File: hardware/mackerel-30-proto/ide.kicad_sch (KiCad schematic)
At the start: 11 parts, among them J12 Screw_Terminal_01x04, J13 Conn_02x20_Odd_Even, U12 74HC245, U13 74HC245

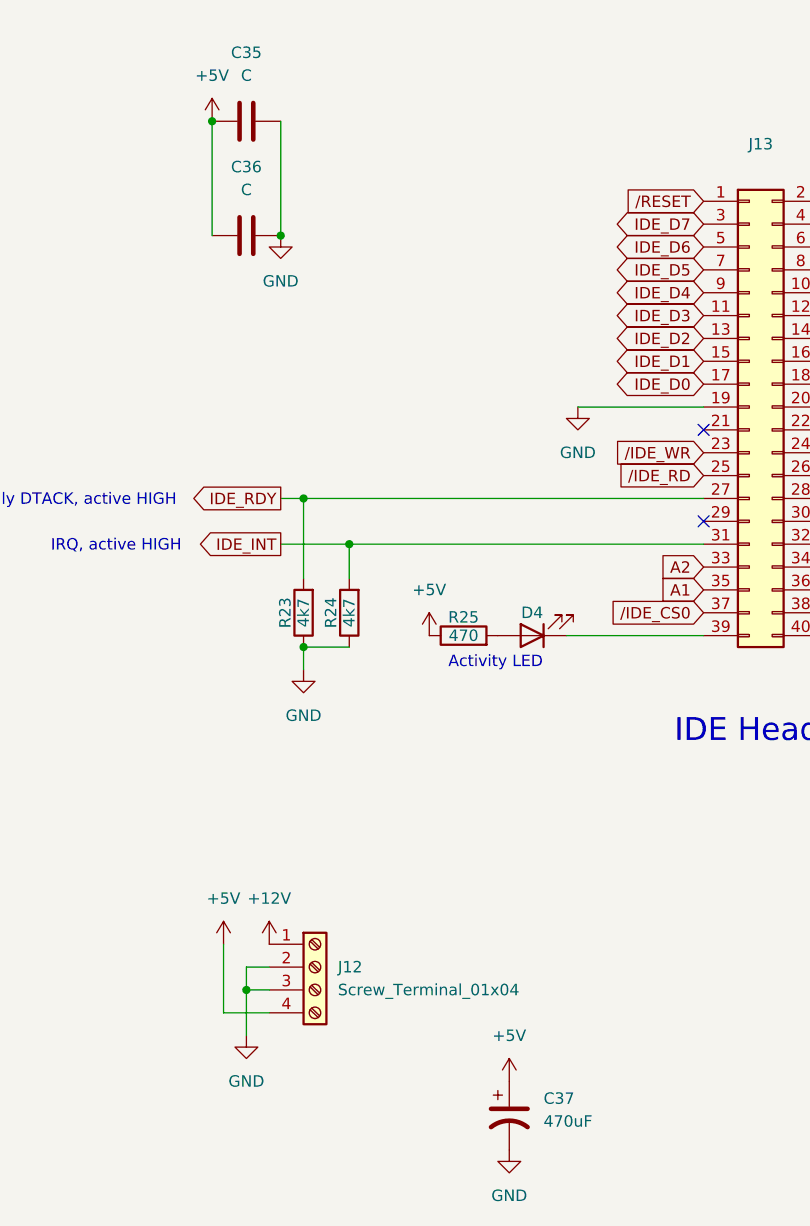
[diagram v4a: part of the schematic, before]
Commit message: Rough routing of data bus to FPU and RAM
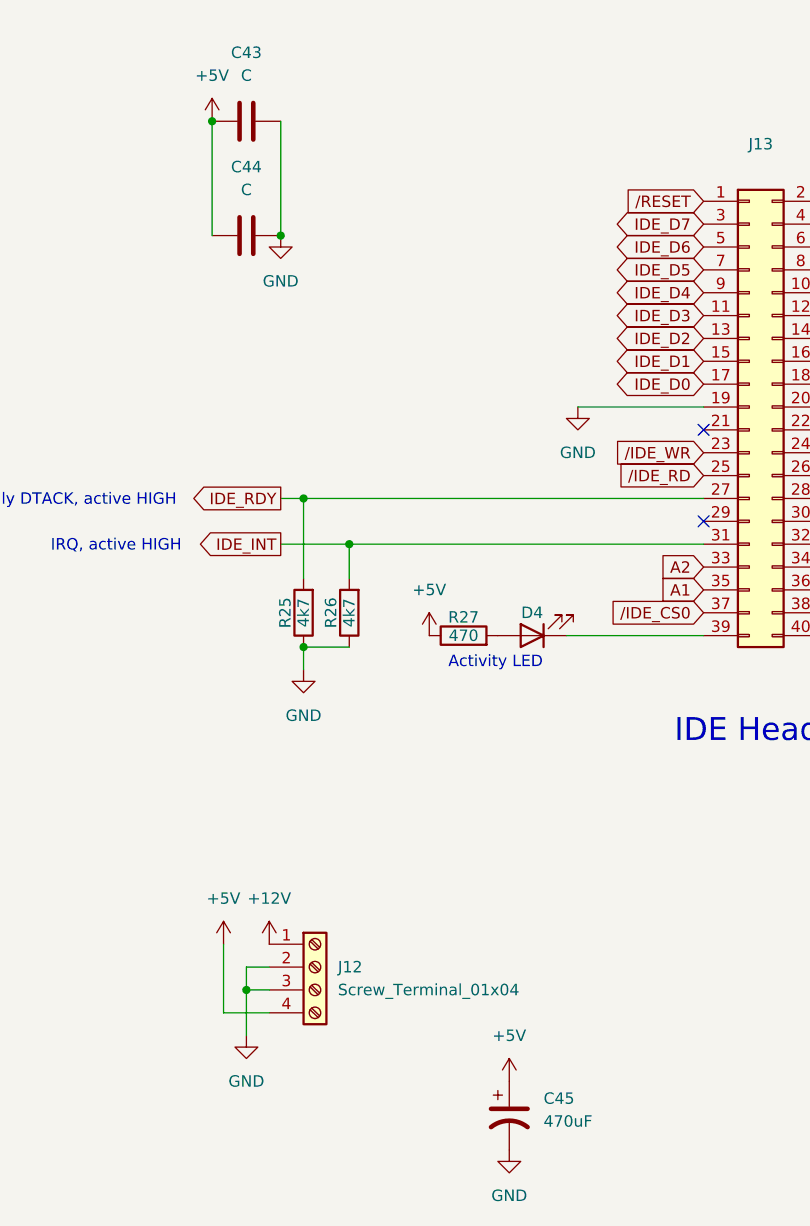
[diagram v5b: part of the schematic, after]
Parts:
- renumbered C35 to C43, C36 to C44, C37 to C45, R23 to R25, R24 to R26, R25 to R27
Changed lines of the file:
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@@
 		(dnp no)
 		(fields_autoplaced yes)
-		(property "Reference" "#PWR084"
+		(property "Reference" "#PWR086"
 			(at 175.26 151.13 0)
 			(effects
@@
 			(project "mackerel-30-proto"
 				(path "/9307474f-ec99-494d-b4c9-fbd0b10ce86a/b80ba0ac-a3c1-4262-b297-c092dfcb6fec"
-					(reference "#PWR084")
+					(reference "#PWR086")
 					(unit 1)
 				)
@@
 		(dnp no)
 		(fields_autoplaced yes)
-		(property "Reference" "#PWR073"
+		(property "Reference" "#PWR075"
 			(at 81.28 39.37 0)
 			(effects
@@
 			(project "mackerel-30-proto"
 				(path "/9307474f-ec99-494d-b4c9-fbd0b10ce86a/b80ba0ac-a3c1-4262-b297-c092dfcb6fec"
-					(reference "#PWR073")
+					(reference "#PWR075")
 					(unit 1)
 				)
@@
 		(dnp no)
 		(fields_autoplaced yes)
-		(property "Reference" "#PWR076"
+		(property "Reference" "#PWR078"
 			(at 81.28 156.21 0)
 			(effects
@@
 			(project "mackerel-30-proto"
 				(path "/9307474f-ec99-494d-b4c9-fbd0b10ce86a/b80ba0ac-a3c1-4262-b297-c092dfcb6fec"
-					(reference "#PWR076")
+					(reference "#PWR078")
 					(unit 1)
 				)
@@
 		(dnp no)
 		(fields_autoplaced yes)
-		(property "Reference" "#PWR087"
+		(property "Reference" "#PWR089"
 			(at 232.41 109.22 0)
 			(effects
@@
 			(project "mackerel-30-proto"
 				(path "/9307474f-ec99-494d-b4c9-fbd0b10ce86a/b80ba0ac-a3c1-4262-b297-c092dfcb6fec"
-					(reference "#PWR087")
+					(reference "#PWR089")
 					(unit 1)
 				)
@@
 		(on_board yes)
 		(dnp no)
-		(property "Reference" "R25"
+		(property "Reference" "R27"
 			(at 170.18 95.758 90)
 			(effects
@@
 			(project "mackerel-30-proto"
 				(path "/9307474f-ec99-494d-b4c9-fbd0b10ce86a/b80ba0ac-a3c1-4262-b297-c092dfcb6fec"
-					(reference "R25")
+					(reference "R27")
 					(unit 1)
 				)
@@
 		(dnp no)
 		(fields_autoplaced yes)
-		(property "Reference" "C37"
+		(property "Reference" "C45"
 			(at 179.07 149.2249 0)
 			(effects
@@
 			(project "mackerel-30-proto"
 				(path "/9307474f-ec99-494d-b4c9-fbd0b10ce86a/b80ba0ac-a3c1-4262-b297-c092dfcb6fec"
-					(reference "C37")
+					(reference "C45")
 					(unit 1)
 				)
@@
 		(dnp no)
 		(fields_autoplaced yes)
-		(property "Reference" "#PWR086"
+		(property "Reference" "#PWR088"
 			(at 182.88 78.74 0)
 			(effects
@@
 			(project "mackerel-30-proto"
 				(path "/9307474f-ec99-494d-b4c9-fbd0b10ce86a/b80ba0ac-a3c1-4262-b297-c092dfcb6fec"
-					(reference "#PWR086")
+					(reference "#PWR088")
 					(unit 1)
 				)
@@
 		(on_board yes)
 		(dnp no)
-		(property "Reference" "R23"
+		(property "Reference" "R25"
 			(at 150.368 95.25 90)
 			(effects
@@
 			(project "mackerel-30-proto"
 				(path "/9307474f-ec99-494d-b4c9-fbd0b10ce86a/b80ba0ac-a3c1-4262-b297-c092dfcb6fec"
-					(reference "R23")
+					(reference "R25")
 					(unit 1)
 				)
@@
 		(dnp no)
 		(fields_autoplaced yes)
-		(property "Reference" "#PWR079"
+		(property "Reference" "#PWR081"
 			(at 146.05 148.59 0)
 			(effects
@@
 			(project "mackerel-30-proto"
 				(path "/9307474f-ec99-494d-b4c9-fbd0b10ce86a/b80ba0ac-a3c1-4262-b297-c092dfcb6fec"
-					(reference "#PWR079")
+					(reference "#PWR081")
 					(unit 1)
 				)
@@
 		(dnp no)
 		(fields_autoplaced yes)
-		(property "Reference" "#PWR077"
+		(property "Reference" "#PWR079"
 			(at 142.24 44.45 0)
 			(effects
@@
 			(project "mackerel-30-proto"
 				(path "/9307474f-ec99-494d-b4c9-fbd0b10ce86a/b80ba0ac-a3c1-4262-b297-c092dfcb6fec"
-					(reference "#PWR077")
+					(reference "#PWR079")
 					(unit 1)
 				)
@@
 		(dnp no)
 		(fields_autoplaced yes)
-		(property "Reference" "#PWR078"
+		(property "Reference" "#PWR080"
 			(at 143.51 135.89 0)
 			(effects
@@
 			(project "mackerel-30-proto"
 				(path "/9307474f-ec99-494d-b4c9-fbd0b10ce86a/b80ba0ac-a3c1-4262-b297-c092dfcb6fec"
-					(reference "#PWR078")
+					(reference "#PWR080")
 					(unit 1)
 				)
@@
 		(dnp no)
 		(fields_autoplaced yes)
-		(property "Reference" "#PWR083"
+		(property "Reference" "#PWR085"
 			(at 166.37 101.6 0)
 			(effects
@@
 			(project "mackerel-30-proto"
 				(path "/9307474f-ec99-494d-b4c9-fbd0b10ce86a/b80ba0ac-a3c1-4262-b297-c092dfcb6fec"
-					(reference "#PWR083")
+					(reference "#PWR085")
 					(unit 1)
 				)
@@
 		(dnp no)
 		(fields_autoplaced yes)
-		(property "Reference" "#PWR085"
+		(property "Reference" "#PWR087"
 			(at 175.26 161.29 0)
 			(effects
@@
 			(project "mackerel-30-proto"
 				(path "/9307474f-ec99-494d-b4c9-fbd0b10ce86a/b80ba0ac-a3c1-4262-b297-c092dfcb6fec"
-					(reference "#PWR085")
+					(reference "#PWR087")
 					(unit 1)
 				)
@@
 		(dnp no)
 		(fields_autoplaced yes)
-		(property "Reference" "C35"
+		(property "Reference" "C43"
 			(at 146.05 33.02 90)
 			(effects
@@
 			(project "mackerel-30-proto"
 				(path "/9307474f-ec99-494d-b4c9-fbd0b10ce86a/b80ba0ac-a3c1-4262-b297-c092dfcb6fec"
-					(reference "C35")
+					(reference "C43")
 					(unit 1)
 				)
@@
 		(dnp no)
 		(fields_autoplaced yes)
-		(property "Reference" "#PWR075"
+		(property "Reference" "#PWR077"
 			(at 81.28 113.03 0)
 			(effects
@@
 			(project "mackerel-30-proto"
 				(path "/9307474f-ec99-494d-b4c9-fbd0b10ce86a/b80ba0ac-a3c1-4262-b297-c092dfcb6fec"
-					(reference "#PWR075")
+					(reference "#PWR077")
 					(unit 1)
 				)
@@
 		(dnp no)
 		(fields_autoplaced yes)
-		(property "Reference" "#PWR082"
+		(property "Reference" "#PWR084"
 			(at 152.4 107.95 0)
 			(effects
@@
 			(project "mackerel-30-proto"
 				(path "/9307474f-ec99-494d-b4c9-fbd0b10ce86a/b80ba0ac-a3c1-4262-b297-c092dfcb6fec"
-					(reference "#PWR082")
+					(reference "#PWR084")
 					(unit 1)
 				)
@@
 		(dnp no)
 		(fields_autoplaced yes)
-		(property "Reference" "#PWR080"
+		(property "Reference" "#PWR082"
 			(at 148.59 135.89 0)
 			(effects
@@
 			(project "mackerel-30-proto"
 				(path "/9307474f-ec99-494d-b4c9-fbd0b10ce86a/b80ba0ac-a3c1-4262-b297-c092dfcb6fec"
-					(reference "#PWR080")
+					(reference "#PWR082")
 					(unit 1)
 				)
@@
 		(dnp no)
 		(fields_autoplaced yes)
-		(property "Reference" "#PWR081"
+		(property "Reference" "#PWR083"
 			(at 149.86 59.69 0)
 			(effects
@@
 			(project "mackerel-30-proto"
 				(path "/9307474f-ec99-494d-b4c9-fbd0b10ce86a/b80ba0ac-a3c1-4262-b297-c092dfcb6fec"
-					(reference "#PWR081")
+					(reference "#PWR083")
 					(unit 1)
 				)
@@
 		(dnp no)
 		(fields_autoplaced yes)
-		(property "Reference" "C36"
+		(property "Reference" "C44"
 			(at 146.05 45.72 90)
 			(effects
@@
 			(project "mackerel-30-proto"
 				(path "/9307474f-ec99-494d-b4c9-fbd0b10ce86a/b80ba0ac-a3c1-4262-b297-c092dfcb6fec"
-					(reference "C36")
+					(reference "C44")
 					(unit 1)
 				)
@@
 		(on_board yes)
 		(dnp no)
-		(property "Reference" "R24"
+		(property "Reference" "R26"
 			(at 155.448 95.25 90)
 			(effects
@@
 			(project "mackerel-30-proto"
 				(path "/9307474f-ec99-494d-b4c9-fbd0b10ce86a/b80ba0ac-a3c1-4262-b297-c092dfcb6fec"
-					(reference "R24")
+					(reference "R26")
 					(unit 1)
 				)
@@
 		(dnp no)
 		(fields_autoplaced yes)
-		(property "Reference" "#PWR074"
+		(property "Reference" "#PWR076"
 			(at 81.28 82.55 0)
 			(effects
@@
 			(project "mackerel-30-proto"
 				(path "/9307474f-ec99-494d-b4c9-fbd0b10ce86a/b80ba0ac-a3c1-4262-b297-c092dfcb6fec"
-					(reference "#PWR074")
-					(unit 1)
-				)
+					(reference "#PWR076")
+					(unit 1)
+				)

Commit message: Mack-30 routed except for expansion header
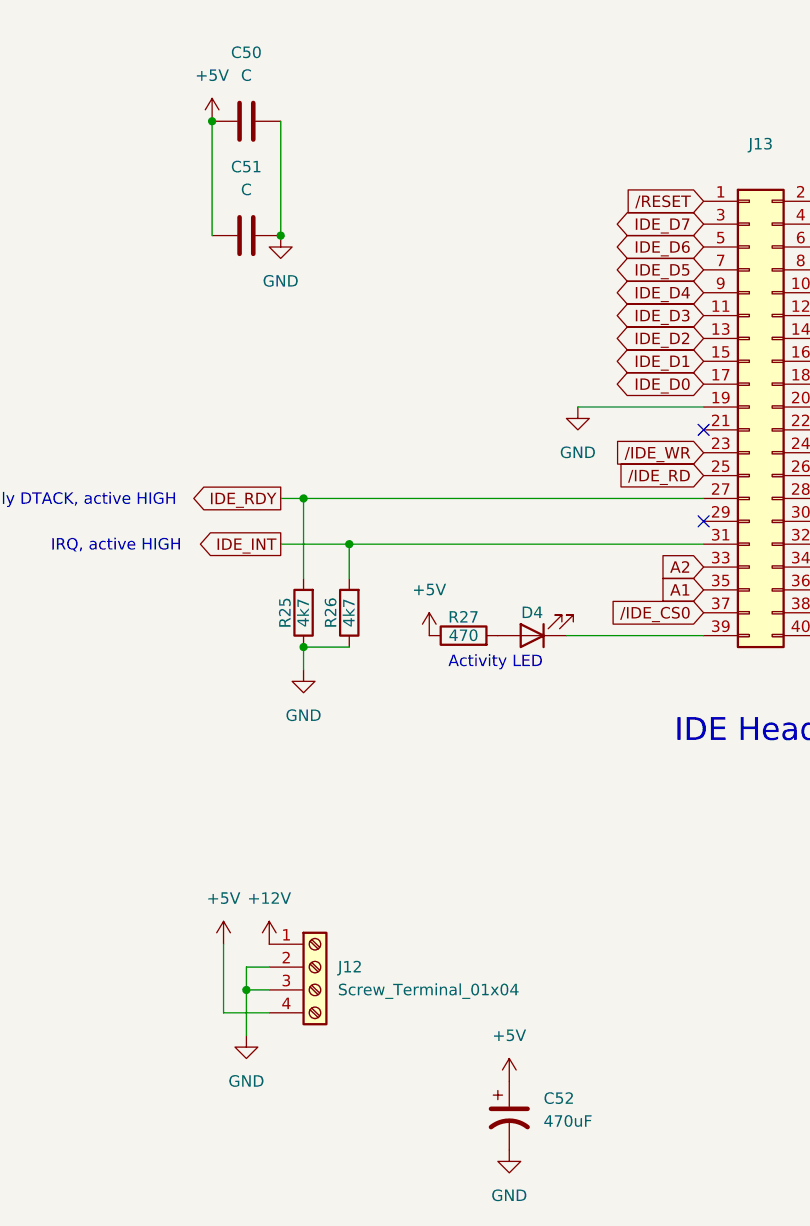
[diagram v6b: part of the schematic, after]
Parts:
- renumbered C43 to C50, C44 to C51, C45 to C52
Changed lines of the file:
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@@
 		(dnp no)
 		(fields_autoplaced yes)
-		(property "Reference" "#PWR086"
+		(property "Reference" "#PWR094"
 			(at 175.26 151.13 0)
 			(effects
@@
 			(project "mackerel-30-proto"
 				(path "/9307474f-ec99-494d-b4c9-fbd0b10ce86a/b80ba0ac-a3c1-4262-b297-c092dfcb6fec"
-					(reference "#PWR086")
+					(reference "#PWR094")
 					(unit 1)
 				)
@@
 		(dnp no)
 		(fields_autoplaced yes)
-		(property "Reference" "#PWR075"
+		(property "Reference" "#PWR083"
 			(at 81.28 39.37 0)
 			(effects
@@
 			(project "mackerel-30-proto"
 				(path "/9307474f-ec99-494d-b4c9-fbd0b10ce86a/b80ba0ac-a3c1-4262-b297-c092dfcb6fec"
-					(reference "#PWR075")
+					(reference "#PWR083")
 					(unit 1)
 				)
@@
 		(dnp no)
 		(fields_autoplaced yes)
-		(property "Reference" "#PWR078"
+		(property "Reference" "#PWR086"
 			(at 81.28 156.21 0)
 			(effects
@@
 			(project "mackerel-30-proto"
 				(path "/9307474f-ec99-494d-b4c9-fbd0b10ce86a/b80ba0ac-a3c1-4262-b297-c092dfcb6fec"
-					(reference "#PWR078")
+					(reference "#PWR086")
 					(unit 1)
 				)
@@
 		(dnp no)
 		(fields_autoplaced yes)
-		(property "Reference" "#PWR089"
+		(property "Reference" "#PWR097"
 			(at 232.41 109.22 0)
 			(effects
@@
 			(project "mackerel-30-proto"
 				(path "/9307474f-ec99-494d-b4c9-fbd0b10ce86a/b80ba0ac-a3c1-4262-b297-c092dfcb6fec"
-					(reference "#PWR089")
+					(reference "#PWR097")
 					(unit 1)
 				)
@@
 		(dnp no)
 		(fields_autoplaced yes)
-		(property "Reference" "C45"
+		(property "Reference" "C52"
 			(at 179.07 149.2249 0)
 			(effects
@@
 			(project "mackerel-30-proto"
 				(path "/9307474f-ec99-494d-b4c9-fbd0b10ce86a/b80ba0ac-a3c1-4262-b297-c092dfcb6fec"
-					(reference "C45")
+					(reference "C52")
 					(unit 1)
 				)
@@
 		(dnp no)
 		(fields_autoplaced yes)
-		(property "Reference" "#PWR088"
+		(property "Reference" "#PWR096"
 			(at 182.88 78.74 0)
 			(effects
@@
 			(project "mackerel-30-proto"
 				(path "/9307474f-ec99-494d-b4c9-fbd0b10ce86a/b80ba0ac-a3c1-4262-b297-c092dfcb6fec"
-					(reference "#PWR088")
+					(reference "#PWR096")
 					(unit 1)
 				)
@@
 		(dnp no)
 		(fields_autoplaced yes)
-		(property "Reference" "#PWR081"
+		(property "Reference" "#PWR089"
 			(at 146.05 148.59 0)
 			(effects
@@
 			(project "mackerel-30-proto"
 				(path "/9307474f-ec99-494d-b4c9-fbd0b10ce86a/b80ba0ac-a3c1-4262-b297-c092dfcb6fec"
-					(reference "#PWR081")
+					(reference "#PWR089")
 					(unit 1)
 				)
@@
 		(dnp no)
 		(fields_autoplaced yes)
-		(property "Reference" "#PWR079"
+		(property "Reference" "#PWR087"
 			(at 142.24 44.45 0)
 			(effects
@@
 			(project "mackerel-30-proto"
 				(path "/9307474f-ec99-494d-b4c9-fbd0b10ce86a/b80ba0ac-a3c1-4262-b297-c092dfcb6fec"
-					(reference "#PWR079")
+					(reference "#PWR087")
 					(unit 1)
 				)
@@
 		(dnp no)
 		(fields_autoplaced yes)
-		(property "Reference" "#PWR080"
+		(property "Reference" "#PWR088"
 			(at 143.51 135.89 0)
 			(effects
@@
 			(project "mackerel-30-proto"
 				(path "/9307474f-ec99-494d-b4c9-fbd0b10ce86a/b80ba0ac-a3c1-4262-b297-c092dfcb6fec"
-					(reference "#PWR080")
+					(reference "#PWR088")
 					(unit 1)
 				)
@@
 		(dnp no)
 		(fields_autoplaced yes)
-		(property "Reference" "#PWR085"
+		(property "Reference" "#PWR093"
 			(at 166.37 101.6 0)
 			(effects
@@
 			(project "mackerel-30-proto"
 				(path "/9307474f-ec99-494d-b4c9-fbd0b10ce86a/b80ba0ac-a3c1-4262-b297-c092dfcb6fec"
-					(reference "#PWR085")
+					(reference "#PWR093")
 					(unit 1)
 				)
@@
 		(dnp no)
 		(fields_autoplaced yes)
-		(property "Reference" "#PWR087"
+		(property "Reference" "#PWR095"
 			(at 175.26 161.29 0)
 			(effects
@@
 			(project "mackerel-30-proto"
 				(path "/9307474f-ec99-494d-b4c9-fbd0b10ce86a/b80ba0ac-a3c1-4262-b297-c092dfcb6fec"
-					(reference "#PWR087")
+					(reference "#PWR095")
 					(unit 1)
 				)
@@
 		(dnp no)
 		(fields_autoplaced yes)
-		(property "Reference" "C43"
+		(property "Reference" "C50"
 			(at 146.05 33.02 90)
 			(effects
@@
 			(project "mackerel-30-proto"
 				(path "/9307474f-ec99-494d-b4c9-fbd0b10ce86a/b80ba0ac-a3c1-4262-b297-c092dfcb6fec"
-					(reference "C43")
+					(reference "C50")
 					(unit 1)
 				)
@@
 		(dnp no)
 		(fields_autoplaced yes)
-		(property "Reference" "#PWR077"
+		(property "Reference" "#PWR085"
 			(at 81.28 113.03 0)
 			(effects
@@
 			(project "mackerel-30-proto"
 				(path "/9307474f-ec99-494d-b4c9-fbd0b10ce86a/b80ba0ac-a3c1-4262-b297-c092dfcb6fec"
-					(reference "#PWR077")
+					(reference "#PWR085")
 					(unit 1)
 				)
@@
 		(dnp no)
 		(fields_autoplaced yes)
-		(property "Reference" "#PWR084"
+		(property "Reference" "#PWR092"
 			(at 152.4 107.95 0)
 			(effects
@@
 			(project "mackerel-30-proto"
 				(path "/9307474f-ec99-494d-b4c9-fbd0b10ce86a/b80ba0ac-a3c1-4262-b297-c092dfcb6fec"
-					(reference "#PWR084")
+					(reference "#PWR092")
 					(unit 1)
 				)
@@
 		(dnp no)
 		(fields_autoplaced yes)
-		(property "Reference" "#PWR082"
+		(property "Reference" "#PWR090"
 			(at 148.59 135.89 0)
 			(effects
@@
 			(project "mackerel-30-proto"
 				(path "/9307474f-ec99-494d-b4c9-fbd0b10ce86a/b80ba0ac-a3c1-4262-b297-c092dfcb6fec"
-					(reference "#PWR082")
+					(reference "#PWR090")
 					(unit 1)
 				)
@@
 		(dnp no)
 		(fields_autoplaced yes)
-		(property "Reference" "#PWR083"
+		(property "Reference" "#PWR091"
 			(at 149.86 59.69 0)
 			(effects
@@
 			(project "mackerel-30-proto"
 				(path "/9307474f-ec99-494d-b4c9-fbd0b10ce86a/b80ba0ac-a3c1-4262-b297-c092dfcb6fec"
-					(reference "#PWR083")
+					(reference "#PWR091")
 					(unit 1)
 				)
@@
 		(dnp no)
 		(fields_autoplaced yes)
-		(property "Reference" "C44"
+		(property "Reference" "C51"
 			(at 146.05 45.72 90)
 			(effects
@@
 			(project "mackerel-30-proto"
 				(path "/9307474f-ec99-494d-b4c9-fbd0b10ce86a/b80ba0ac-a3c1-4262-b297-c092dfcb6fec"
-					(reference "C44")
+					(reference "C51")
 					(unit 1)
 				)
@@
 		(dnp no)
 		(fields_autoplaced yes)
-		(property "Reference" "#PWR076"
+		(property "Reference" "#PWR084"
 			(at 81.28 82.55 0)
 			(effects
@@
 			(project "mackerel-30-proto"
 				(path "/9307474f-ec99-494d-b4c9-fbd0b10ce86a/b80ba0ac-a3c1-4262-b297-c092dfcb6fec"
-					(reference "#PWR076")
-					(unit 1)
-				)
+					(reference "#PWR084")
+					(unit 1)
+				)

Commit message: PCB cleanup
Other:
- title: Mackerel-30 Proto -> Mackerel-30
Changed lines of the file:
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@@
 	(paper "A")
 	(title_block
-		(title "Mackerel-30 Proto")
-		(date "2024-10-05")
-		(rev "1.0")
+		(title "Mackerel-30")
+		(date "2024-11-09")
+		(rev "0.1")
 		(company "Colin Maykish")
 	)

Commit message: Mackerel-30 v0.1 PCB release
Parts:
- C50, C51: value C -> 0.1uF
- R27: value 470 -> 1k
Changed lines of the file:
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@@
 			)
 		)
-		(property "Value" "470"
+		(property "Value" "1k"
 			(at 170.18 97.79 90)
 			(effects
@@
 			)
 		)
-		(property "Value" "C"
+		(property "Value" "0.1uF"
 			(at 146.05 35.56 90)
 			(effects
@@
 			)
 		)
-		(property "Value" "C"
+		(property "Value" "0.1uF"
 			(at 146.05 48.26 90)
 			(effects
